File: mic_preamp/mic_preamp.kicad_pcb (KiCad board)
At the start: 2 copper layers, 64 x 38.4 mm, 30 parts, among them J1 Conn_01x03, J2 JACK_STEREO, J3 Conn_01x03, J4 Conn_01x01, U1 INA217

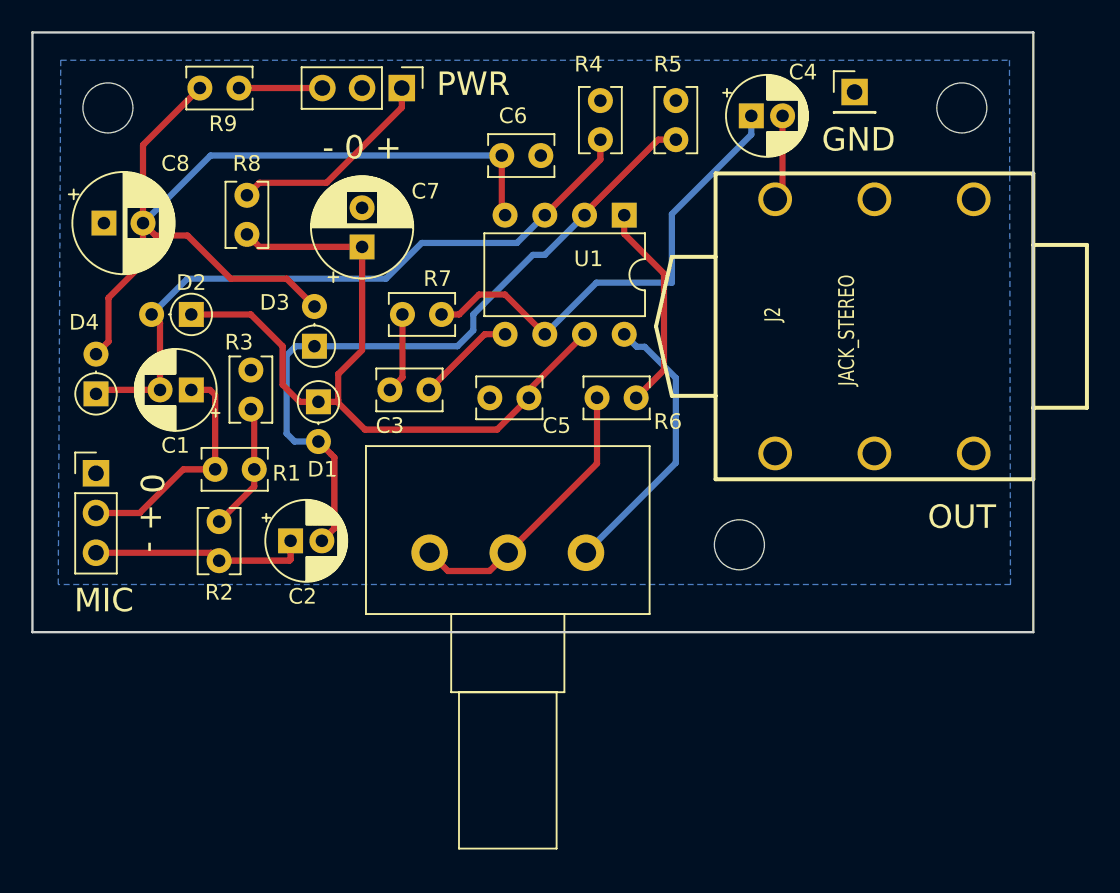
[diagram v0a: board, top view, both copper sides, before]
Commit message: Minor changes to the INA-217 based mic preamp
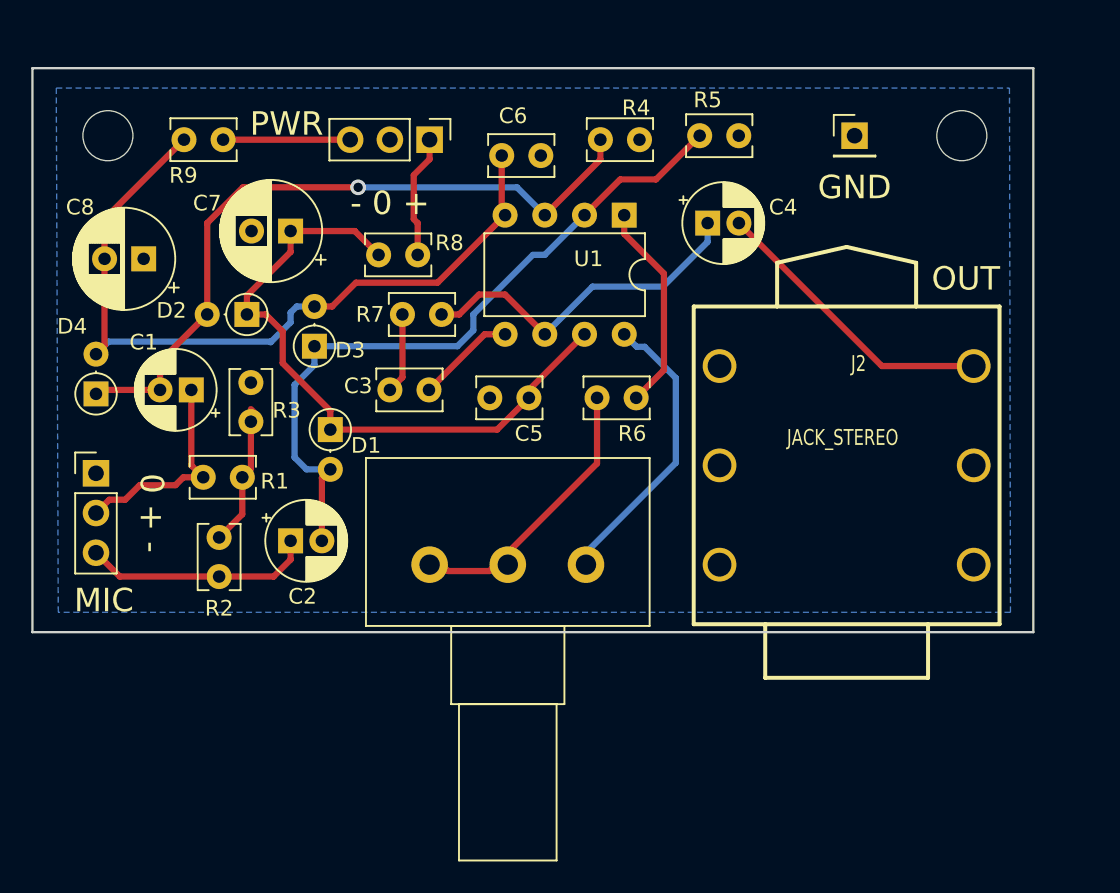
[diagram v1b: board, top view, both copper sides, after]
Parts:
- removed H3: MountingHole, MountingHole:MountingHole_3.2mm_M3
- moved H1 29.8 mm to (146.1, 104.9)
- moved R8 11.6 mm to (111.3, 112.5), turned to 180 degrees
- moved J2 8.87 mm to (138.4, 126.0), turned to 90 degrees
- moved C4 7.41 mm to (129.8, 110.5)
- moved C7 4.68 mm to (103.1, 111.0), turned to 180 degrees
- moved J3 3.75 mm to (112.0, 105.2)
- moved D2 3.56 mm to (100.3, 116.3)
- moved R9 3.45 mm to (98.8, 105.2)
- moved C8 3.42 mm to (93.7, 112.8), turned to 180 degrees
- moved J4 2.79 mm to (139.2, 104.9)
- moved D1 1.93 mm to (105.7, 123.7)
- moved H2 1.78 mm to (91.4, 104.9)
- moved R5 1.55 mm to (129.3, 104.9), turned to 0 degrees
- moved R2 1.02 mm to (98.6, 133.1)
- moved R1 0.92 mm to (97.5, 126.7)
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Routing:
- net Net-(C4-Pad2): track 5.53 -> 18.8 mm
- net -15V: track 61.6 -> 50.2 mm
- net +15V: track 50.7 -> 42.1 mm
- net Net-(C4-Pad1): track 30.5 -> 22.2 mm
- net Net-(J3-Pad1): track 13.5 -> 7.89 mm
- net Net-(J3-Pad3): track 5.33 -> 8.13 mm
- net Net-(C1-Pad2): track 43.3 -> 45.7 mm, vias 0 -> 1
- net Net-(C1-Pad1): track 15.2 -> 13.7 mm
- net Net-(C2-Pad1): track 13.9 -> 14.7 mm
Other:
- board size 64 x 38.4 mm -> 64 x 36.1 mm
